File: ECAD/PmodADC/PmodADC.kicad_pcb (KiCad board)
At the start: 4 copper layers, 143 parts, among them J1 AudioIn, J2 LeaderTech SMS405, J3 Pmod, J4 AudioIn, U1 74VHC595BQ,115, U10 MIC5270BM5, U11 SN74LVC1G17DCK, U12 OPA1602, U13 LT1711xMS8, U16 LF398_SOIC8, U2 74VHC595BQ,115, U20 74AHCT541BQ,115, U3 TLV61046ADB, U4 TPS63700, U5 74AHCV541ABQ, U6 74AHCV541ABQ, U7 REF3450, U8 LDK320AM-R, U9 LDK320AM-R

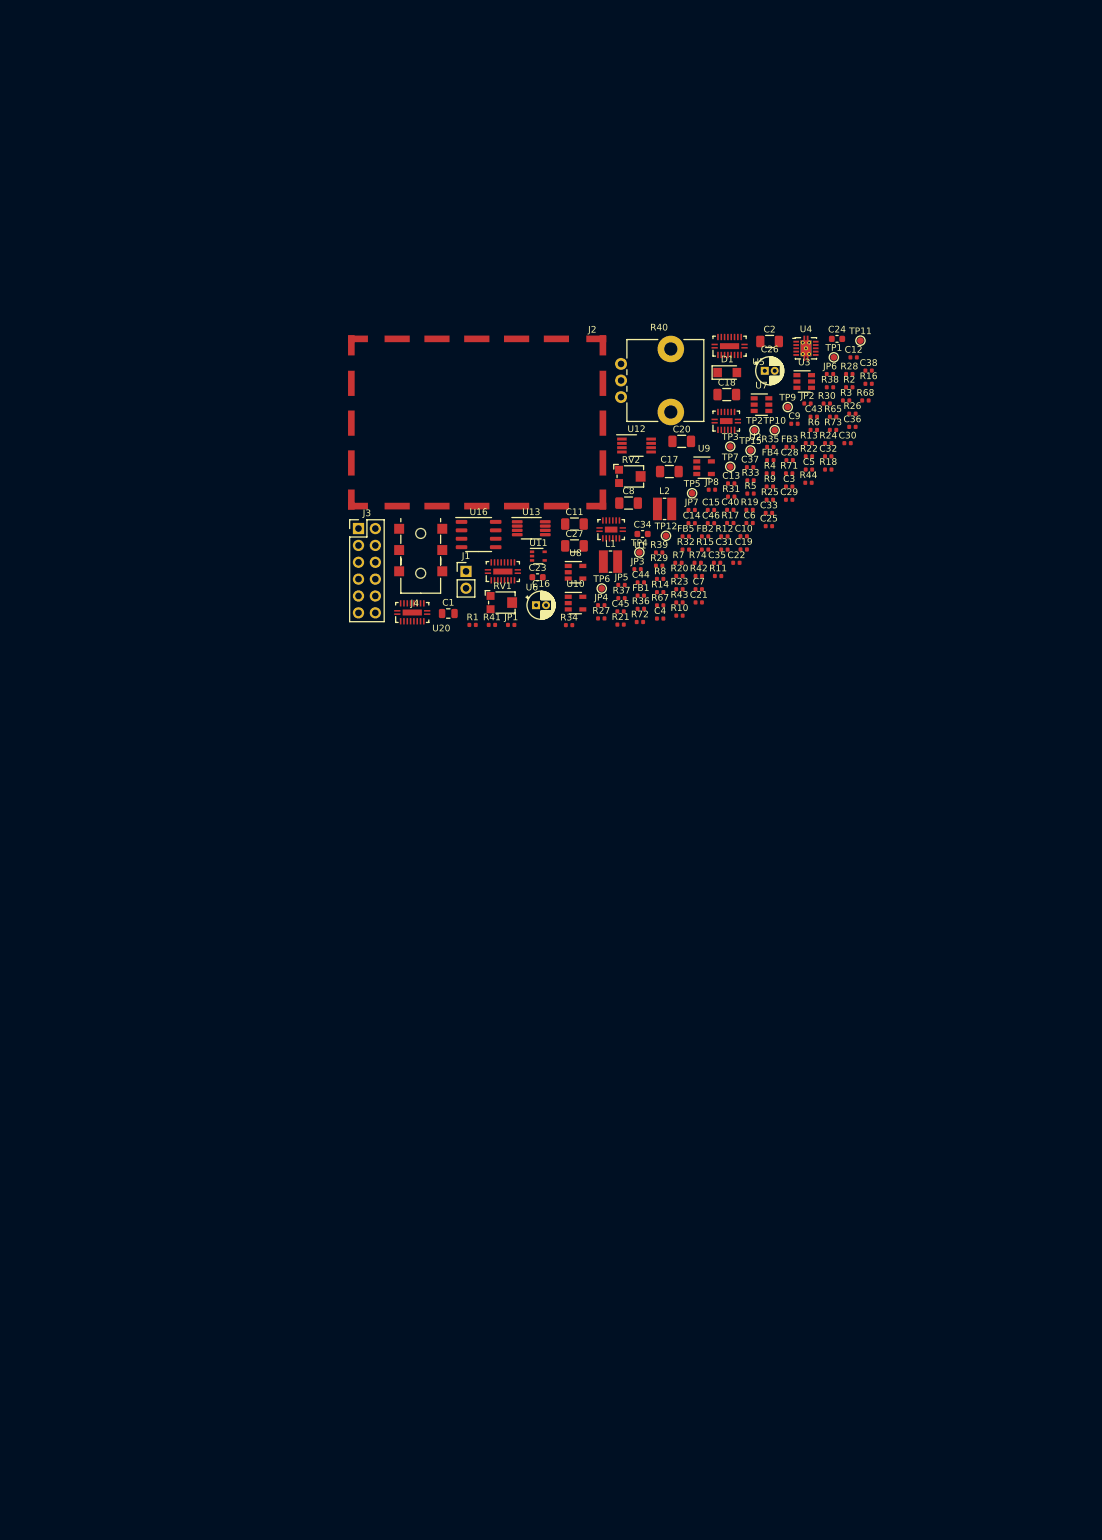
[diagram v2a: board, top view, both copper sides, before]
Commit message: First Draft Layout PmodADC done
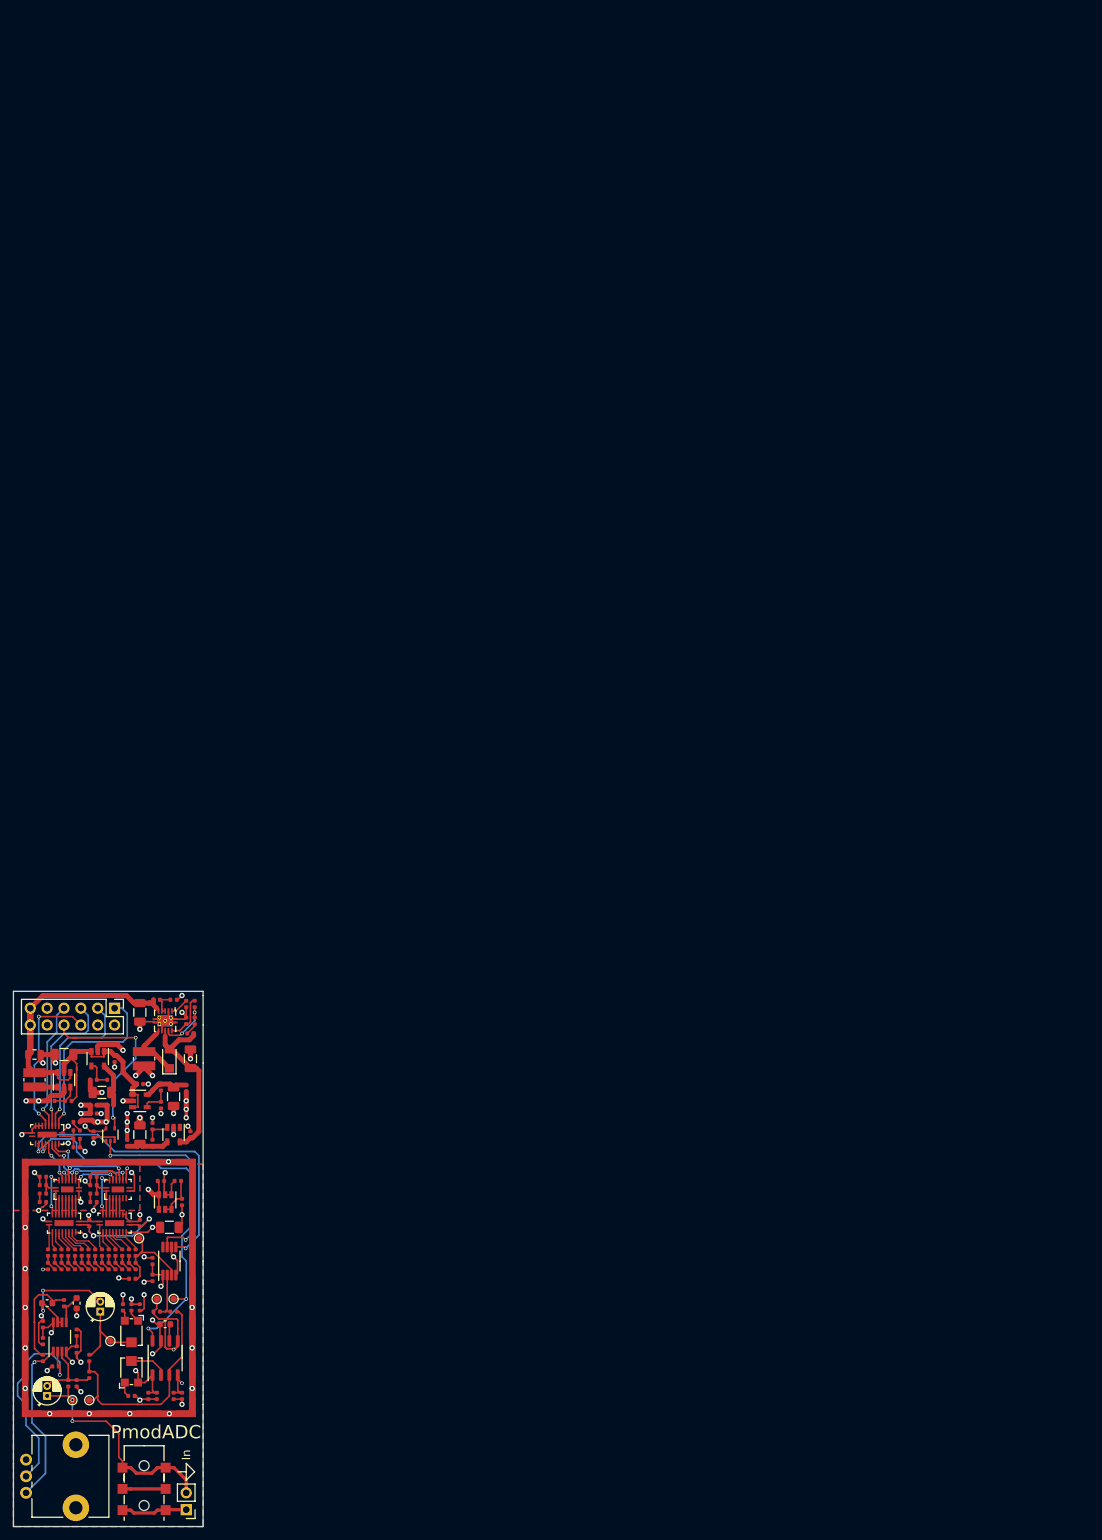
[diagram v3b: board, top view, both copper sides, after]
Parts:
- removed TP1: S&H, TestPoint:TestPoint_Pad_D1.0mm
- removed TP12, TP15, TP4, TP7: GND, TestPoint:TestPoint_Pad_D1.0mm
- removed TP2: DAC, TestPoint:TestPoint_Pad_D1.0mm
- moved R38 188.2 mm to (-125.7, 78.1), turned to 270 degrees
- moved R40 187.9 mm to (-133.3, 94.6)
- moved JP6 185.6 mm to (-123.8, 74.3), turned to 270 degrees
- moved C24 185.0 mm to (-125.7, 66.0), turned to 90 degrees
- moved TP9 182.9 mm to (-123.8, 80.6), turned to 90 degrees
- moved R65 181.5 mm to (-117.5, 80.0), turned to 180 degrees
- moved C36 179.7 mm to (-125.7, 70.5), turned to 270 degrees
- moved TP11 179.1 mm to (-113.7, 65.4), turned to 180 degrees
- moved C30 177.3 mm to (-113.7, 80.0), turned to 270 degrees
- moved R28 176.0 mm to (-122.9, 60.5), turned to 90 degrees
- moved R16 175.9 mm to (-124.0, 58.4), turned to 90 degrees
- moved TP3 174.6 mm to (-126.4, 80.6), turned to 90 degrees
- moved C28 174.0 mm to (-130.8, 71.8), turned to 270 degrees
- moved C26 173.5 mm to (-122.2, 67.3), turned to 90 degrees
- moved R26 173.1 mm to (-125.0, 60.5), turned to 90 degrees
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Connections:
- C10 pad 2: GND -> GNDA
- C12 pad 1: GND -> GNDA
- C13 pad 1: GND -> GNDA
- C14 pad 2: GND -> GNDA
- C17 pad 2: GND -> GNDA
- C18 pad 2: GND -> GNDA
- C20 pad 1: GND -> GNDA
- C22 pad 1: GND -> GNDA
- C24 pad 1: GND -> GNDA
- C25 pad 2: GND -> GNDA
- C27 pad 2: GND -> GNDA
- C28 pad 2: GND -> GNDA
- C29 pad 1: GND -> GNDA
- C30 pad 2: GND -> GNDA
- C31 pad 2: GND -> GNDA
- C32 pad 2: GND -> GNDA
- C33 pad 2: GND -> GNDA
- C34 pad 2: GND -> GNDA
- C35 pad 2: GND -> GNDA
- C36 pad 1: GND -> GNDA
- C37 pad 2: GND -> GNDA
- C38 pad 1: +5V -> +5VA
- C38 pad 2: GND -> GNDA
- C40 pad 1: +5V -> +5VA
- C40 pad 2: GND -> GNDA
- C43 pad 2: GND -> GNDA
- C44 pad 2: GND -> GNDA
- C9 pad 2: GND -> GNDA
- J1 pad 1: GND -> GNDA
- J2 pad 1: GND -> GNDA
- J3 pad 10: GND -> GNDA
- J4 pad S: GND -> GNDA
- R33 pad 2: GND -> GNDA
- R35 pad 2: GND -> GNDA
- R36 pad 2: GND -> GNDA
- R38 pad 2: GND -> GNDA
- R39 pad 1: GND -> GNDA
- R44 pad 1: GND -> GNDA
- R65 pad 1: GND -> GNDA
- R9 pad 2: GND -> GNDA
- U10 pad 1: (no net) -> Net-(U10-Pad1)
- U10 pad 2: GND -> GNDA
- U10 pad 3: Net-(U10-Pad3) -> Net-(R36-Pad1)
- U13 pad 1: +5V -> +5VA
- U13 pad 4: GND -> GNDA
- U13 pad 5: /COMP_L_5v -> /COMP_L
- U13 pad 6: GND -> GNDA
- U16 pad 7: GND -> GNDA
- U20 pad 10: Net-(U20-Pad10) -> GND
- U5 pad 1: GND -> GNDA
- U5 pad 10: GND -> GNDA
- U5 pad 19: GND -> GNDA
- U6 pad 1: GND -> GNDA
- U6 pad 10: GND -> GNDA
- U6 pad 19: GND -> GNDA
- U6 pad 2: GND -> GNDA
- U6 pad 3: GND -> GNDA
- U7 pad 1: GND -> GNDA
- U7 pad 2: GND -> GNDA
- U8 pad 2: GND -> GNDA
- U9 pad 2: GND -> GNDA
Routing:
- net GNDA: track 0.00 -> 217.3 mm, vias 0 -> 47
- net +5VA: track 0.00 -> 103.4 mm, vias 0 -> 3
- net -5V: track 0.00 -> 100.6 mm, vias 0 -> 5
- net +9V: track 0.00 -> 84.9 mm, vias 0 -> 6
- net GND: track 0.00 -> 75.9 mm, vias 0 -> 20
- net +3V3: track 0.00 -> 62.4 mm, vias 0 -> 1
- net /S&H: track 0.00 -> 59.0 mm, vias 0 -> 3
- net +5V: track 0.00 -> 54.6 mm, vias 0 -> 6
- net /COMP_L: track 0.00 -> 45.0 mm, vias 0 -> 2
- net /Vref_5V: track 0.00 -> 42.9 mm, vias 0 -> 4
- net Net-(C16-Pad1): track 0.00 -> 34.8 mm, vias 0 -> 2
- net Net-(JP5-Pad2): track 0.00 -> 34.0 mm
- net /COMP: track 0.00 -> 31.9 mm, vias 0 -> 2
- net Net-(R39-Pad2): track 0.00 -> 31.5 mm, vias 0 -> 1
- net Net-(C12-Pad2): track 0.00 -> 30.9 mm
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- added copper zone on In2.Cu, net GND
- added copper zone on B.Cu, net GNDA
- added copper zone on F.Cu, net GNDA
- added copper zone on In2.Cu, net GNDA
- added copper zone on In1.Cu, net Net-(JP7-Pad1)
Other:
- board outline added: 28.6 x 80.6 mm
- net class Default: clearance 0.2 -> 0.13
- rule trace_clearance: 0.2 -> 0.13
- board text added: "In"
- board text added: "PmodADC"
- board text added: "SCHILK"
- board text added: "v0.2"
